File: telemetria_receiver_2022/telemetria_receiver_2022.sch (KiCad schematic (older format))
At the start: 44 parts, among them J2 Conn_01x06_Male, J4 USB_B_Mini, SW1 SW_Push, U1 NRF24L01_Breakout, U2 DS3231M, U3 STM32L4P5RET6, U4 LM1117-3.3, Y1 Crystal(100MHZ)?

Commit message: added logos lib, fixed routing, impedance matching of spi and sdio, removed external RTC, PCB rearrangement
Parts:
- removed C12: 100nF, Capacitor_SMD:C_0603_1608Metric, symbol Device:C_Small
- removed FB1: 100R@100MHz, Inductor_SMD:L_0603_1608Metric, symbol Device:Ferrite_Bead_Small
- removed R1, R2: 4.7kR, Resistor_SMD:R_0603_1608Metric, symbol Device:R
- removed R3, R4: 10kR, Resistor_SMD:R_0603_1608Metric, symbol Device:R
- removed U2: DS3231M, Package_SO:SOIC-16W_7.5x10.3mm_P1.27mm, symbol Timer_RTC:DS3231M
- J4: symbol Connector:USB_B_Mini -> telemetria_receiver_2022-rescue:USB_B_Mini-Connector
- U3: symbol STM32L4P5RET6:STM32L4P5RET6 -> telemetria_receiver_2022-rescue:STM32L4P5RET6-STM32L4P5RET6
- U4: footprint Package_TO_SOT_SMD:SOT-223 -> Package_TO_SOT_SMD:SOT-223-3_TabPin2
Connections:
- no-connect marks 28 -> 27
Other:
- note removed: "RTC Supply / Battery"
- note removed: "Real-Time Clock"

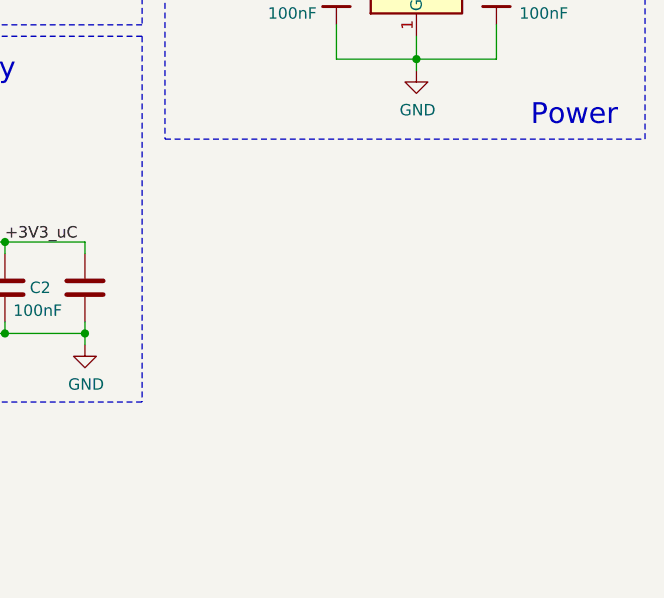
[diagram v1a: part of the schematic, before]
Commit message: controlled impedance tracks, added mounting holes
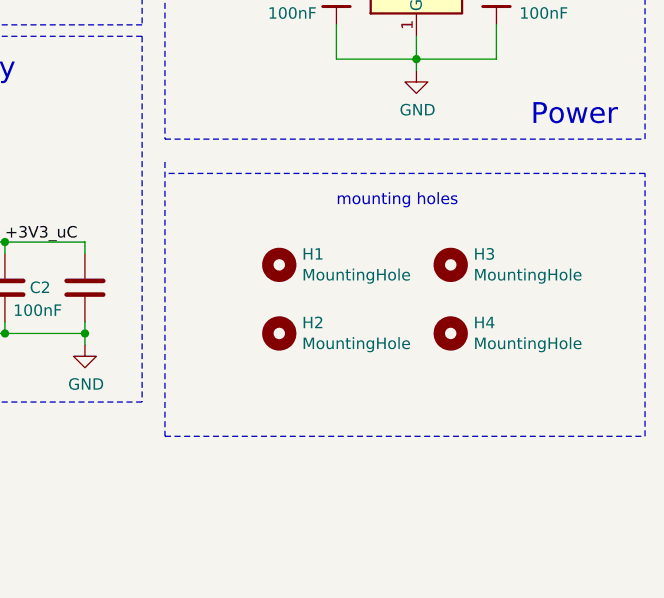
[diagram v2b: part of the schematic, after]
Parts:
- added H1, H2, H3, H4: MountingHole, MountingHole:MountingHole_3.2mm_M3_Pad, symbol Mechanical:MountingHole
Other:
- note added: "mounting holes\n"
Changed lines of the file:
@@
 EESchema Schematic File Version 4
 LIBS:telemetria_receiver_2022-cache
-EELAYER 29 0
+EELAYER 30 0
 EELAYER END
 $Descr A4 11693 8268
@@
 Wire Wire Line
 	3400 1500 3450 1500
+$Comp
+L Mechanical:MountingHole H1
+U 1 1 6224147F
+P 9550 4450
+F 0 "H1" H 9650 4496 50  0000 L CNN
+F 1 "MountingHole" H 9650 4405 50  0000 L CNN
+F 2 "MountingHole:MountingHole_3.2mm_M3_Pad" H 9550 4450 50  0001 C CNN
+F 3 "~" H 9550 4450 50  0001 C CNN
+	1    9550 4450
+	1    0    0    -1
+$EndComp
+$Comp
+L Mechanical:MountingHole H2
+U 1 1 62242341
+P 9550 4750
+F 0 "H2" H 9650 4796 50  0000 L CNN
+F 1 "MountingHole" H 9650 4705 50  0000 L CNN
+F 2 "MountingHole:MountingHole_3.2mm_M3_Pad" H 9550 4750 50  0001 C CNN
+F 3 "~" H 9550 4750 50  0001 C CNN
+	1    9550 4750
+	1    0    0    -1
+$EndComp
+$Comp
+L Mechanical:MountingHole H3
+U 1 1 622500A4
+P 10300 4450
+F 0 "H3" H 10400 4496 50  0000 L CNN
+F 1 "MountingHole" H 10400 4405 50  0000 L CNN
+F 2 "MountingHole:MountingHole_3.2mm_M3_Pad" H 10300 4450 50  0001 C CNN
+F 3 "~" H 10300 4450 50  0001 C CNN
+	1    10300 4450
+	1    0    0    -1
+$EndComp
+$Comp
+L Mechanical:MountingHole H4
+U 1 1 6225D50E
+P 10300 4750
+F 0 "H4" H 10400 4796 50  0000 L CNN
+F 1 "MountingHole" H 10400 4705 50  0000 L CNN
+F 2 "MountingHole:MountingHole_3.2mm_M3_Pad" H 10300 4750 50  0001 C CNN
+F 3 "~" H 10300 4750 50  0001 C CNN
+	1    10300 4750
+	1    0    0    -1
+$EndComp
+Wire Notes Line
+	9050 4000 9050 5200
+Wire Notes Line
+	9050 5200 11150 5200
+Wire Notes Line
+	11150 5200 11150 4050
+Wire Notes Line
+	11150 4050 9050 4050
+Text Notes 9800 4200 0    50   ~ 0
+mounting holes\n
 $EndSCHEMATC
